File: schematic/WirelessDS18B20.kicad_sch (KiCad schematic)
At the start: 10 parts, among them P2 1-Wire Bus, Q1 BS170, U1 WeMos_mini, U2 AMS1117-3.3

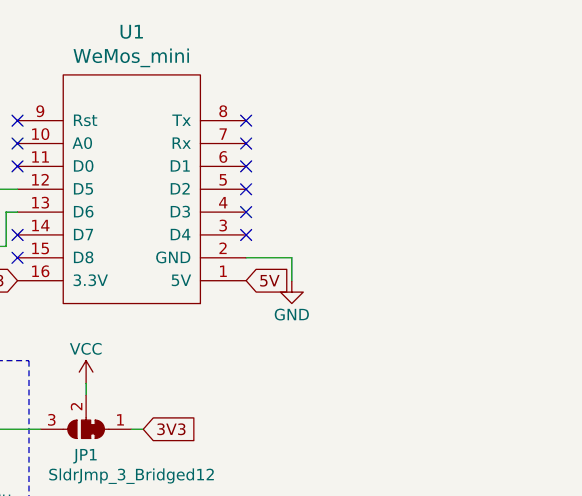
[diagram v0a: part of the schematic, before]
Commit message: Add PWR_FLAG to schematic
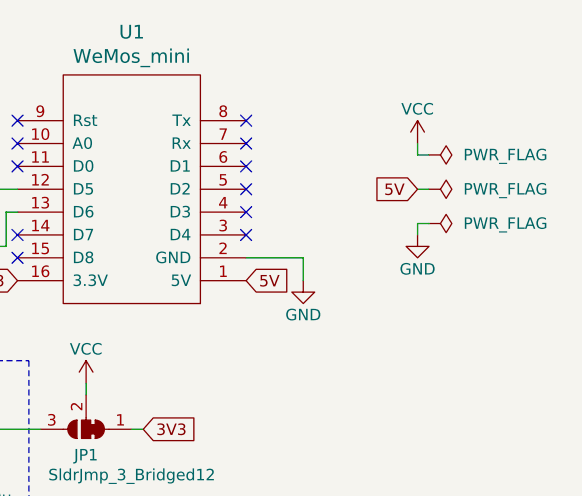
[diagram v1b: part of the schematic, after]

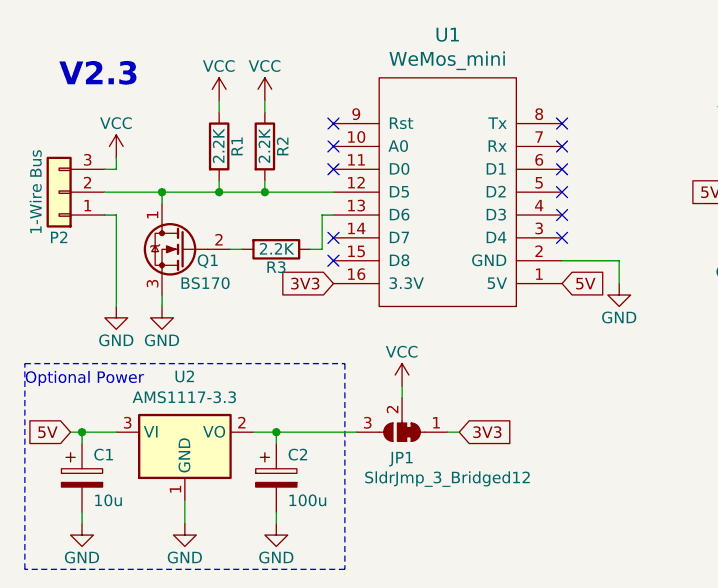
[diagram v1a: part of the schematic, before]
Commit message: V3.0 of the PCB (additional power is not optional)
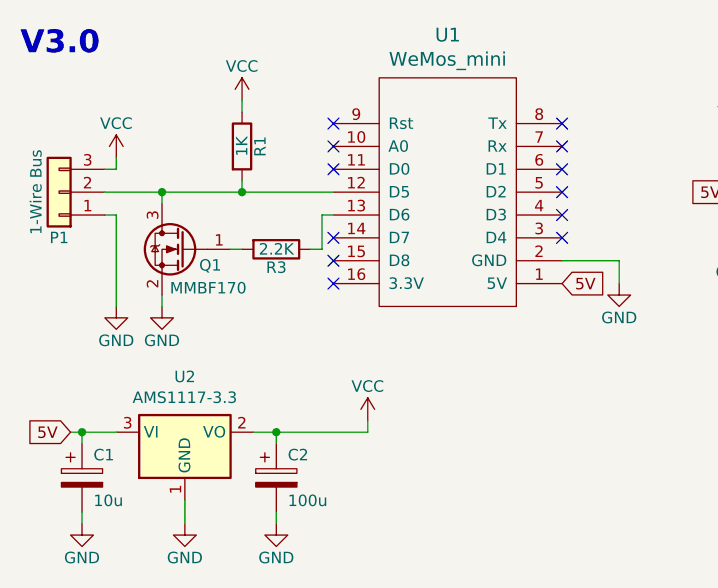
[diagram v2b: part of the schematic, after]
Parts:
- removed JP1: SldrJmp_3_Bridged12, Jumper:SolderJumper-3_P1.3mm_Bridged12_Pad1.0x1.5mm_NumberLabels, symbol Jumper:SolderJumper_3_Bridged12
- removed Q1: BS170, Package_TO_SOT_THT:TO-92_Inline_Horizontal2, symbol Transistor_FET:BS170
- removed R2: 2.2K, Resistor_SMD:R_0805_2012Metric_Pad1.15x1.40mm_HandSolder, symbol Device:R
- added Q1: MMBF170, Package_TO_SOT_SMD:SOT-23_Handsoldering, symbol Transistor_FET:MMBF170
- R1: value 2.2K -> 1K; footprint Resistor_SMD:R_0805_2012Metric_Pad1.15x1.40mm_HandSolder -> Resistor_SMD:R_0805_2012Metric_Pad1.20x1.40mm_HandSolder
- R3: footprint Resistor_SMD:R_0805_2012Metric_Pad1.15x1.40mm_HandSolder -> Resistor_SMD:R_0805_2012Metric_Pad1.20x1.40mm_HandSolder
- renumbered P2 to P1
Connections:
- net GND: now also Q1.2 (S)
- net VCC: now also C2.1, U2.2 (VO)
- net at P1.2 (Pin_2), R1.2, U1.12 (D5): now also Q1.3 (D)
- net at R3.2: now also Q1.1 (G)
- net 3V3: no longer names the net of U1.16 (3.3V)
- no-connect marks 11 -> 12
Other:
- note added: "V3.0"
- note removed: "Optional Power"
- note removed: "V2.3"
- moved on the sheet: R1

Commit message: Update of schematic
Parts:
- removed Q1: MMBF170, Package_TO_SOT_SMD:SOT-23_Handsoldering, symbol Transistor_FET:MMBF170
- added Q1: 2N7002, Package_TO_SOT_SMD:SOT-23_Handsoldering, symbol Transistor_FET:2N7002
- C1: LCSC (none) -> C119052
- C2: LCSC (none) -> C129289
- P1, U1: now left out of the parts list
- R1: LCSC (none) -> C17513
- R3: LCSC (none) -> C17520
- U2: LCSC (none) -> C6186
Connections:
- net GND: now also Q1.2 (S)
- net at P1.2 (Pin_2), R1.2, U1.12 (D5): now also Q1.3 (D)
- net at R3.2: now also Q1.1 (G)
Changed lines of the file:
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@@
 		(unit 1)
 		(exclude_from_sim no)
-		(in_bom yes)
+		(in_bom no)
 		(on_board yes)
 		(dnp no)
@@
 			)
 		)
+		(property "LCSC" "C17513"
+			(at 40.64 29.21 90)
+			(effects
+				(font
+					(size 1.27 1.27)
+				)
+				(hide yes)
+			)
+		)
 		(pin "1"
 		)
@@
 			)
 		)
+		(property "LCSC" "C17520"
+			(at 44.45 40.64 90)
+			(effects
+				(font
+					(size 1.27 1.27)
+				)
+				(hide yes)
+			)
+		)
 		(pin "2"
 		)
@@
 		(unit 1)
 		(exclude_from_sim no)
-		(in_bom yes)
+		(in_bom no)
 		(on_board yes)
 		(dnp no)
@@
 			)
 		)
+		(property "LCSC" "C119052"
+			(at 22.86 66.04 0)
+			(effects
+				(font
+					(size 1.27 1.27)
+				)
+				(hide yes)
+			)
+		)
 		(pin "1"
 		)
@@
 			)
 		)
+		(property "LCSC" "C129289"
+			(at 44.45 66.04 0)
+			(effects
+				(font
+					(size 1.27 1.27)
+				)
+				(hide yes)
+			)
+		)
 		(pin "2"
 		)
@@
 		)
 		(property "Description" ""
+			(at 34.29 60.96 0)
+			(effects
+				(font
+					(size 1.27 1.27)
+				)
+				(hide yes)
+			)
+		)
+		(property "LCSC" "C6186"
 			(at 34.29 60.96 0)
 			(effects
@@
 	)
 	(symbol
-		(lib_id "Transistor_FET:MMBF170")
-		(at 34.29 40.64 0)
-		(mirror y)
-		(unit 1)
-		(exclude_from_sim no)
-		(in_bom yes)
-		(on_board yes)
-		(dnp no)
-		(property "Reference" "Q1"
-			(at 38.354 42.418 0)
-			(effects
-				(font
-					(size 1.27 1.27)
-				)
-				(justify left)
-			)
-		)
-		(property "Value" "MMBF170"
-			(at 41.148 44.958 0)
-			(effects
-				(font
-					(size 1.27 1.27)
-				)
-				(justify left)
-			)
-		)
-		(property "Footprint" "Package_TO_SOT_SMD:SOT-23_Handsoldering"
-			(at 29.21 42.545 0)
-			(effects
-				(font
-					(size 1.27 1.27)
-					(italic yes)
-				)
-				(justify left)
-				(hide yes)
-			)
-		)
-		(property "Datasheet" "https://www.diodes.com/assets/Datasheets/ds30104.pdf"
-			(at 29.21 44.45 0)
-			(effects
-				(font
-					(size 1.27 1.27)
-				)
-				(justify left)
-				(hide yes)
-			)
-		)
-		(property "Description" "0.5A Id, 60V Vds, N-Channel MOSFET, SOT-23"
-			(at 34.29 40.64 0)
-			(effects
-				(font
-					(size 1.27 1.27)
-				)
-				(hide yes)
-			)
-		)
-		(pin "1"
-		)
-		(pin "3"
-		)
-		(pin "2"
-		)
-		(instances
-			(project ""
-				(path "/5f7cbbe3-ef5c-49a8-8769-c89d21be606b"
-					(reference "Q1")
-					(unit 1)
-				)
-			)
-		)
-	)
-	(symbol
 		(lib_id "power:PWR_FLAG")
 		(at 96.52 38.1 270)
@@
 					(unit 1)
 				)
+			)
+		)
+	)
+	(symbol
+		(lib_id "Transistor_FET:2N7002")
+		(at 34.29 40.64 0)
+		(mirror y)
+		(unit 1)
+		(exclude_from_sim no)
+		(in_bom yes)
+		(on_board yes)
+		(dnp no)
+		(property "Reference" "Q1"
+			(at 38.1 42.672 0)
+			(effects
+				(font
+					(size 1.27 1.27)
+				)
+				(justify left)
+			)
+		)
+		(property "Value" "2N7002"
+			(at 39.878 44.958 0)
+			(effects
+				(font
+					(size 1.27 1.27)
+				)
+				(justify left)
+			)
+		)
+		(property "Footprint" "Package_TO_SOT_SMD:SOT-23_Handsoldering"
+			(at 29.21 42.545 0)
+			(effects
+				(font
+					(size 1.27 1.27)
+					(italic yes)
+				)
+				(justify left)
+				(hide yes)
+			)
+		)
+		(property "Datasheet" "https://www.onsemi.com/pub/Collateral/NDS7002A-D.PDF"
+			(at 29.21 44.45 0)
+			(effects
+				(font
+					(size 1.27 1.27)
+				)
+				(justify left)
+				(hide yes)
+			)
+		)
+		(property "Description" "0.115A Id, 60V Vds, N-Channel MOSFET, SOT-23"
+			(at 34.29 40.64 0)
+			(effects
+				(font
+					(size 1.27 1.27)
+				)
+				(hide yes)
+			)
+		)
+		(property "LCSC" "C8545"
+			(at 34.29 40.64 0)
+			(effects
+				(font
+					(size 1.27 1.27)
+				)
+				(hide yes)
+			)
+		)
+		(pin "1"
+		)
+		(pin "2"
+		)
+		(pin "3"
+		)
+		(instances
+			(project ""
+				(path "/5f7cbbe3-ef5c-49a8-8769-c89d21be606b"
+					(reference "Q1")
+					(unit 1)
+				)

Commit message: Update schematic
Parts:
- C1: LCSC C119052 -> C7171
- C2: LCSC C129289 -> C16133
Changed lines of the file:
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@@
 			)
 		)
-		(property "LCSC" "C119052"
+		(property "LCSC" "C7171"
 			(at 22.86 66.04 0)
 			(effects
@@
 			)
 		)
-		(property "LCSC" "C129289"
+		(property "LCSC" "C16133"
 			(at 44.45 66.04 0)
 			(effects

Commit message: Update schematic
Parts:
- added Q2: 2N7002, Package_TO_SOT_SMD:SOT-23_Handsoldering, symbol Transistor_FET:2N7002
- R2: renamed from R3; value 2.2K -> 3.3K; LCSC C17520 -> C26010
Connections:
- net GND: now also Q2.2 (S)
- net VCC: now also R2.1
- net at P1.2 (Pin_2), R1.2, U1.12 (D5): now also Q2.3 (D); no longer Q1.3 (D)
- net at U1.13 (D6): now also Q1.1 (G); no longer R2.1
- net at R2.2: now also Q1.3 (D), Q2.1 (G); no longer Q1.1 (G)
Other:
- moved on the sheet: C1, C2, Q1, R1, R2, U1, U2

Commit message: Update schematic
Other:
- note added: "V3.1"
- note removed: "V3.0"
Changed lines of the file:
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@@
 		)
 	)
-	(text "V3.0"
+	(text "V3.1"
 		(exclude_from_sim no)
 		(at 16.002 19.304 0)

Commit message: Update schematic and PCB
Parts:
- removed P1: 1-Wire Bus, TerminalBlock:TerminalBlock_bornier-3_P5.08mm, symbol Connector_Generic:Conn_01x03
- removed U1: WeMos_mini, wemos_d1_mini:wemos-d1-mini-DIL-only, symbol wemos_mini:WeMos_mini
- added J1: WeMos_mini_Hat_Left, wemos_d1_mini:WeMos_D1_mini_Hat_Left, symbol wemos_mini:WeMos_D1_mini_Hat_Left
- added J2: WeMos_mini_Hat_Right, wemos_d1_mini:WeMos_D1_mini_Hat_Right, symbol wemos_mini:WeMos_D1_mini_Hat_Right
- added J3: 1-Wire Bus, TerminalBlock:TerminalBlock_bornier-3_P5.08mm, symbol Connector:Screw_Terminal_01x03
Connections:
- net 5V: now also J1.8 (5V)
- net GND: now also J1.7 (GND), J3.1 (Pin_1)
- net VCC: now also J3.3 (Pin_3)
- net at Q2.3 (D), R1.2: now also J2.4 (D5), J3.2 (Pin_2)
- net at Q1.1 (G): now also J2.5 (D6)
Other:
- moved on the sheet: C1, C2, Q1, Q2, R1, R2, U2
